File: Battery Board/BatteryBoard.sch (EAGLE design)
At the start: 27 parts, among them J0 1725656, Q1 IAUC60N04S6L030HATMA1, U0 STM32L031K4U6, U1 MCP73831T-2ATI_OT, U2 MP2152GQFU-33-P, U3 STM809TWX6F

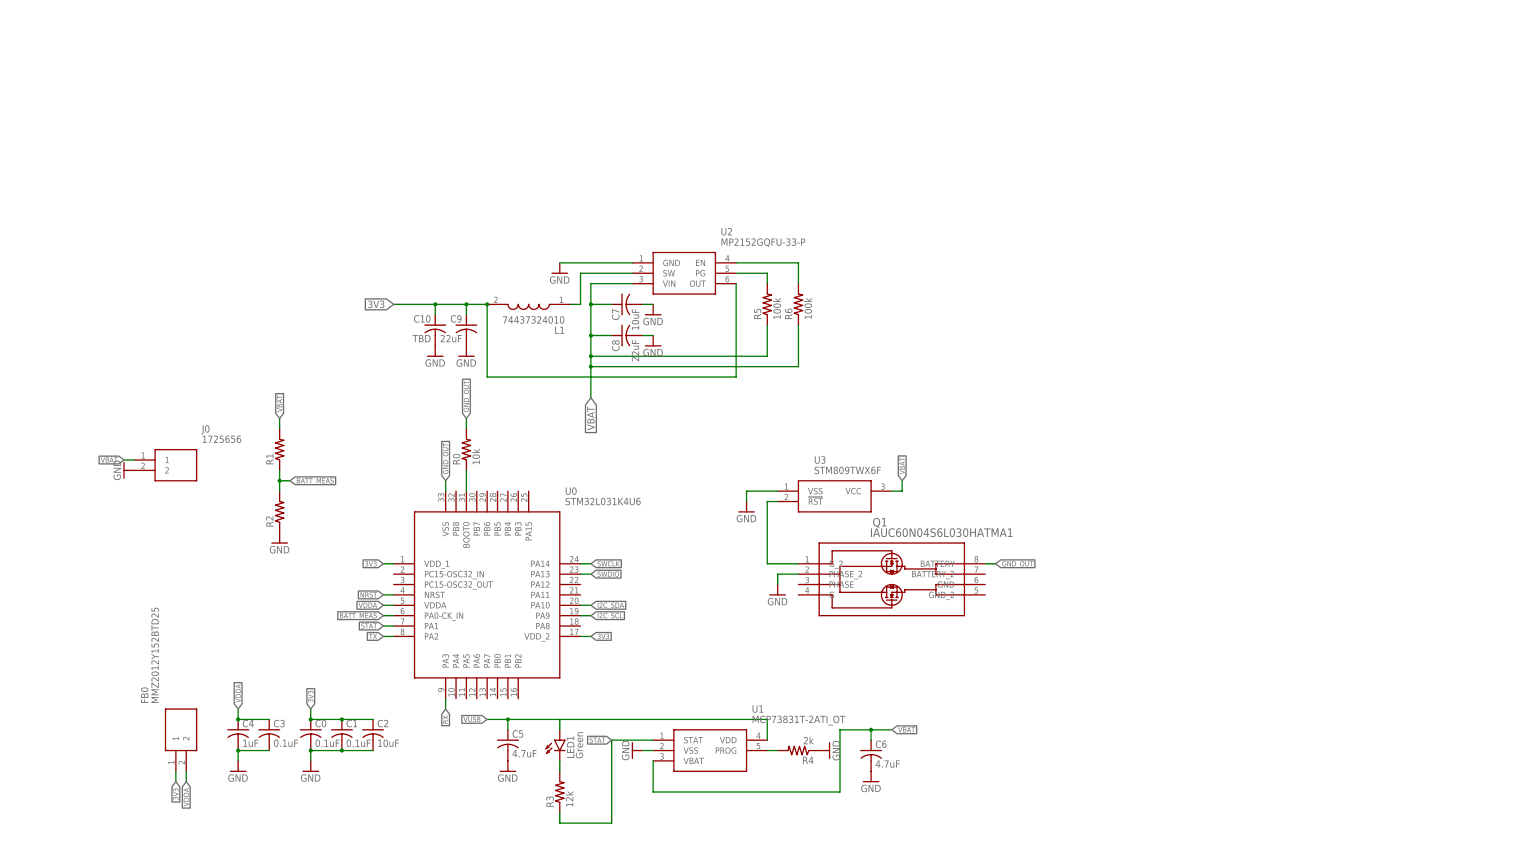
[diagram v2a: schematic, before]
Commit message: Boost/Buck Completed, PCB Started
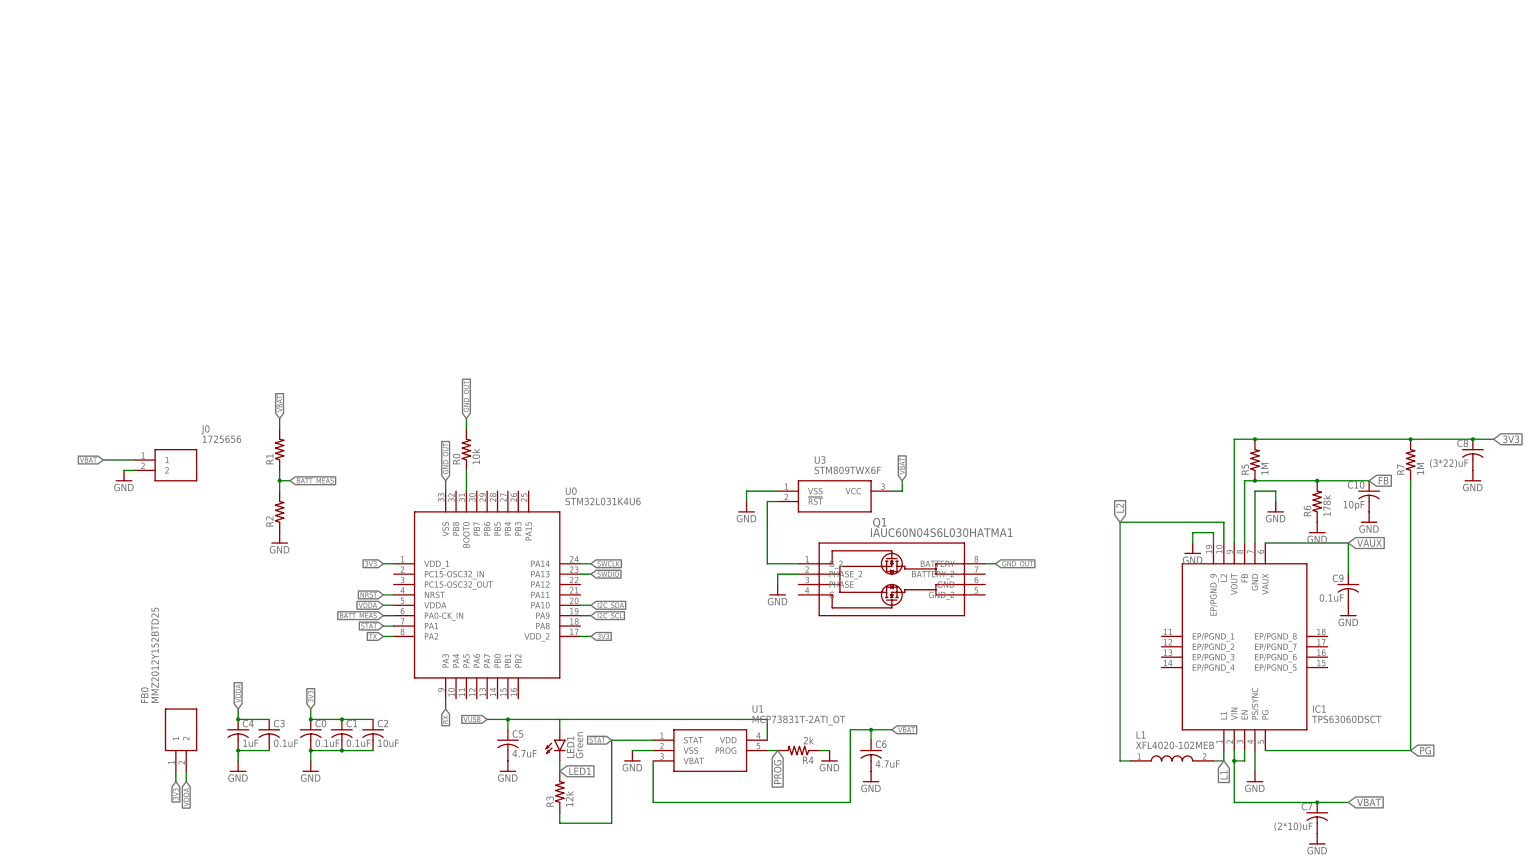
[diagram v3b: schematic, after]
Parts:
- removed U2: MP2152GQFU-33-P, SamacSys_Parts:MP2152GQFU-33-P
- added IC1: TPS63060DSCT, SamacSys_Parts:TPS63060DSCT
- added R7: 1M, rcl:R-US_R0805
- C10: value TBD -> 10pF
- C7: value 10uF -> (2*10)uF
- C8: value 22uF -> (3*22)uF
- C9: value 22uF -> 0.1uF
- L1: value 74437324010 -> XFL4020-102MEB; device SamacSys_Parts:74437324010 -> SamacSys_Parts:XFL4020-102MEB
- R5: value 100k -> 1M
- R6: value 100k -> 178k
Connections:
- net N$2 renamed LED1
- net N$4 renamed PROG
- removed net L1-SW: L1.1, U2.SW
- removed net N$5: R5.2, U2.PG
- removed net N$6: R6.2, U2.EN
- new net FB: C10.1, IC1.FB, R5.1, R6.2
- new net L1: IC1.L1, L1.2
- new net L2: IC1.L2, L1.1
- new net PG: IC1.PG, R7.1
- new net VAUX: C9.1, IC1.VAUX
- net 3V3: now also C8.1, IC1.VOUT, R5.2, R7.2; no longer C10.1, C9.1, L1.2, U2.OUT
- net GND: now also IC1.EP/PGND_9, IC1.GND, IC1.PS/SYNC, R6.1; no longer U2.GND
- net VBAT: now also IC1.EN, IC1.VIN; no longer C8.1, R5.1, R6.1, U2.VIN
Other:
- moved on the sheet: C10, C7, C8, C9, L1, R5, R6

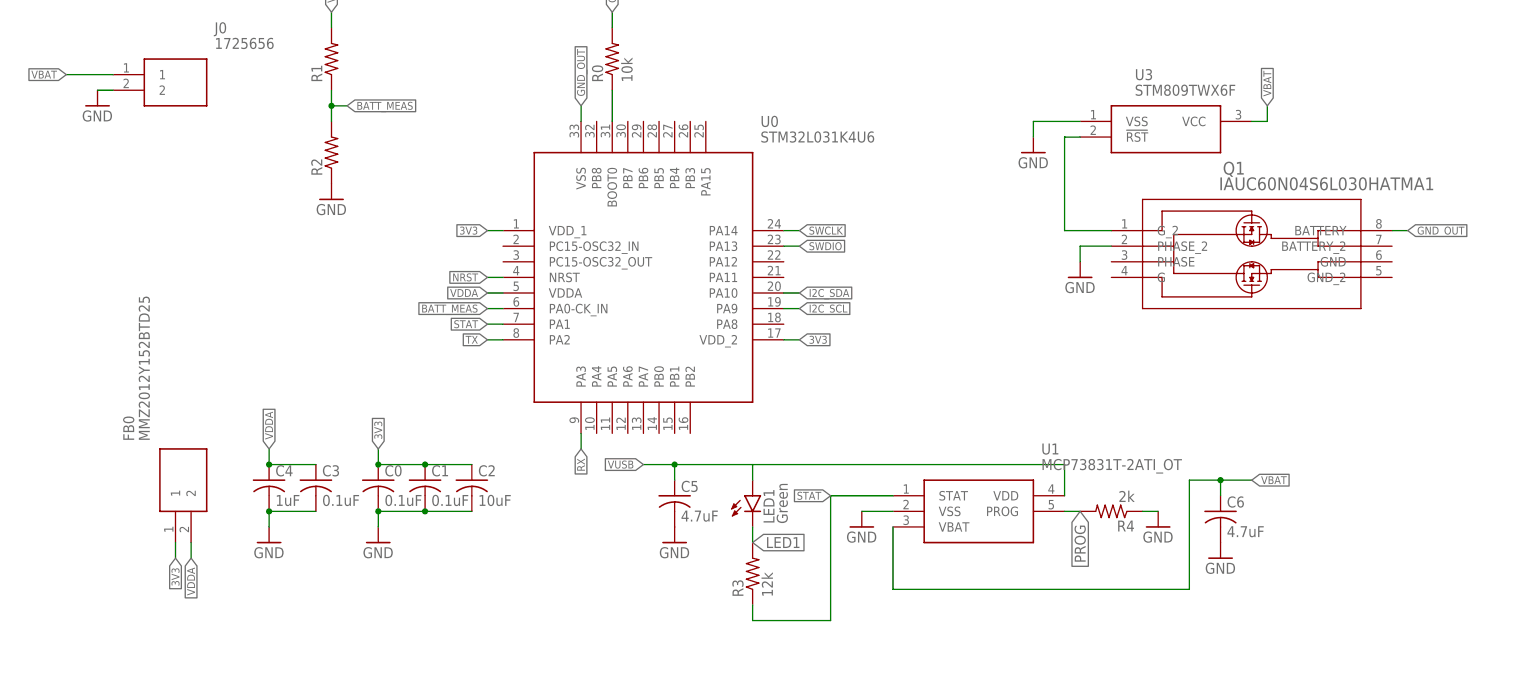
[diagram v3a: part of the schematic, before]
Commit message: added switch jumper
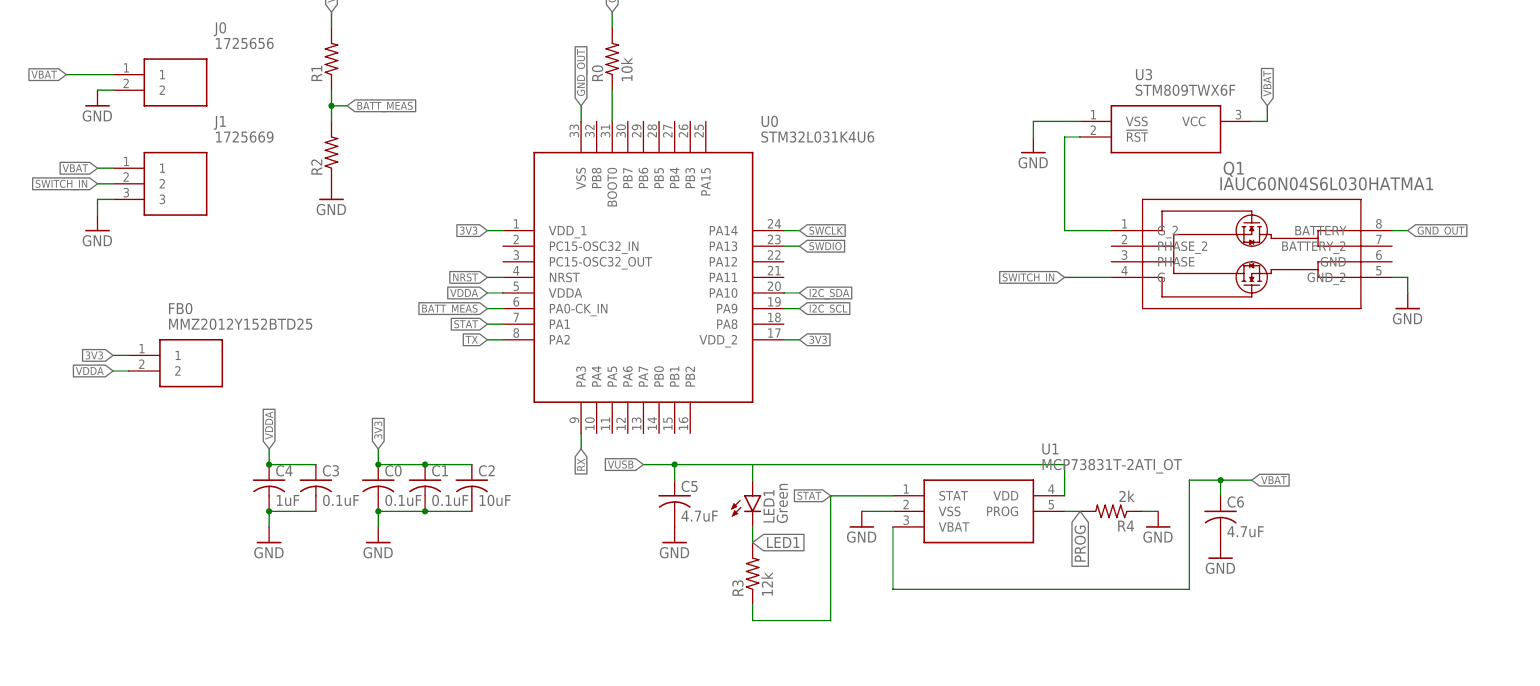
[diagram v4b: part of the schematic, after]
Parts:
- added J1: 1725669, SamacSys_Parts:1725669
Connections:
- new net SWITCH_IN: J1.2, Q1.G
- net GND: now also J1.3, Q1.GND_2; no longer Q1.PHASE_2
- net VBAT: now also J1.1
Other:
- moved on the sheet: FB0
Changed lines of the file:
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@@
 <part name="C7" library="rcl" library_urn="urn:adsk.eagle:library:334" deviceset="C-US" device="C0805" package3d_urn="urn:adsk.eagle:package:23617/2" value="(2*10)uF"/>
 <part name="GND23" library="supply1" library_urn="urn:adsk.eagle:library:371" deviceset="GND" device=""/>
+<part name="J1" library="SamacSys_Parts" deviceset="1725669" device=""/>
+<part name="GND1" library="supply1" library_urn="urn:adsk.eagle:library:371" deviceset="GND" device=""/>
 </parts>
 <sheets>
@@
 <attribute name="VALUE" x="-25.4" y="-2.54" size="1.778" layer="96"/>
 </instance>
-<instance part="FB0" gate="G$1" x="-38.1" y="0" smashed="yes" rot="R90">
-<attribute name="NAME" x="-45.72" y="16.51" size="1.778" layer="95" rot="R90" align="center-left"/>
-<attribute name="VALUE" x="-43.18" y="16.51" size="1.778" layer="96" rot="R90" align="center-left"/>
+<instance part="FB0" gate="G$1" x="-45.72" y="30.48" smashed="yes">
+<attribute name="NAME" x="-39.37" y="38.1" size="1.778" layer="95" align="center-left"/>
+<attribute name="VALUE" x="-39.37" y="35.56" size="1.778" layer="96" align="center-left"/>
 </instance>
 <instance part="R1" gate="G$1" x="-12.7" y="78.74" smashed="yes" rot="R90">
@@
 <attribute name="VALUE" x="99.06" y="60.96" size="1.778" layer="96"/>
 </instance>
-<instance part="GND11" gate="1" x="109.22" y="43.18" smashed="yes">
-<attribute name="VALUE" x="106.68" y="40.64" size="1.778" layer="96"/>
+<instance part="GND11" gate="1" x="162.56" y="38.1" smashed="yes">
+<attribute name="VALUE" x="160.02" y="35.56" size="1.778" layer="96"/>
 </instance>
 <instance part="Q1" gate="A" x="111.76" y="50.8" smashed="yes">
@@
 <instance part="GND23" gate="1" x="241.3" y="-17.78" smashed="yes">
 <attribute name="VALUE" x="238.76" y="-20.32" size="1.778" layer="96"/>
+</instance>
+<instance part="J1" gate="G$1" x="-48.26" y="60.96" smashed="yes">
+<attribute name="NAME" x="-31.75" y="68.58" size="1.778" layer="95" align="center-left"/>
+<attribute name="VALUE" x="-31.75" y="66.04" size="1.778" layer="96" align="center-left"/>
+</instance>
+<instance part="GND1" gate="1" x="-50.8" y="50.8" smashed="yes">
+<attribute name="VALUE" x="-53.34" y="48.26" size="1.778" layer="96"/>
 </instance>
 </instances>
@@
 </segment>
 <segment>
-<pinref part="Q1" gate="A" pin="PHASE_2"/>
-<wire x1="114.3" y1="48.26" x2="109.22" y2="48.26" width="0.1524" layer="91"/>
-<pinref part="GND11" gate="1" pin="GND"/>
-<wire x1="109.22" y1="48.26" x2="109.22" y2="45.72" width="0.1524" layer="91"/>
-</segment>
-<segment>
 <pinref part="IC1" gate="G$1" pin="EP/PGND_9"/>
 <wire x1="215.9" y1="55.88" x2="215.9" y2="58.42" width="0.1524" layer="91"/>
@@
 <pinref part="C7" gate="G$1" pin="2"/>
 <pinref part="GND23" gate="1" pin="GND"/>
+</segment>
+<segment>
+<pinref part="Q1" gate="A" pin="GND_2"/>
+<wire x1="160.02" y1="43.18" x2="162.56" y2="43.18" width="0.1524" layer="91"/>
+<pinref part="GND11" gate="1" pin="GND"/>
+<wire x1="162.56" y1="43.18" x2="162.56" y2="40.64" width="0.1524" layer="91"/>
+</segment>
+<segment>
+<pinref part="J1" gate="G$1" pin="3"/>
+<wire x1="-48.26" y1="55.88" x2="-50.8" y2="55.88" width="0.1524" layer="91"/>
+<wire x1="-50.8" y1="55.88" x2="-50.8" y2="53.34" width="0.1524" layer="91"/>
+<pinref part="GND1" gate="1" pin="GND"/>
 </segment>
 </net>
@@
 <segment>
 <pinref part="FB0" gate="G$1" pin="2"/>
-<wire x1="-35.56" y1="0" x2="-35.56" y2="-2.54" width="0.1524" layer="91"/>
-<label x="-35.56" y="-2.54" size="1.27" layer="95" rot="R270" xref="yes"/>
+<wire x1="-45.72" y1="27.94" x2="-48.26" y2="27.94" width="0.1524" layer="91"/>
+<label x="-48.26" y="27.94" size="1.27" layer="95" rot="R180" xref="yes"/>
 </segment>
 </net>
@@
 <label x="248.92" y="-7.62" size="1.778" layer="95" xref="yes"/>
 </segment>
+<segment>
+<pinref part="J1" gate="G$1" pin="1"/>
+<wire x1="-48.26" y1="60.96" x2="-50.8" y2="60.96" width="0.1524" layer="91"/>
+<label x="-50.8" y="60.96" size="1.27" layer="95" rot="R180" xref="yes"/>
+</segment>
 </net>
 <net name="I2C_SDA" class="0">
@@
 <segment>
 <pinref part="FB0" gate="G$1" pin="1"/>
-<wire x1="-38.1" y1="0" x2="-38.1" y2="-2.54" width="0.1524" layer="91"/>
-<label x="-38.1" y="-2.54" size="1.27" layer="95" rot="R270" xref="yes"/>
+<wire x1="-45.72" y1="30.48" x2="-48.26" y2="30.48" width="0.1524" layer="91"/>
+<label x="-48.26" y="30.48" size="1.27" layer="95" rot="R180" xref="yes"/>
 </segment>
 <segment>
@@
 </segment>
 </net>
+<net name="SWITCH_IN" class="0">
+<segment>
+<pinref part="Q1" gate="A" pin="G"/>
+<wire x1="114.3" y1="43.18" x2="106.68" y2="43.18" width="0.1524" layer="91"/>
+<label x="106.68" y="43.18" size="1.27" layer="95" rot="R180" xref="yes"/>
+</segment>
+<segment>
+<pinref part="J1" gate="G$1" pin="2"/>
+<wire x1="-48.26" y1="58.42" x2="-50.8" y2="58.42" width="0.1524" layer="91"/>
+<label x="-50.8" y="58.42" size="1.27" layer="95" rot="R180" xref="yes"/>
+</segment>
+</net>
